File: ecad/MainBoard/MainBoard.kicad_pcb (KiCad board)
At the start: 2 copper layers, 34.6 x 88.7 mm, 44 parts, among them IC1 RC4558, J1 ACJM-HHDR, J2 ACJM-HHDR, J3 PJ-102A, Q1 2N4401BU, Q2 2N4401BU, SW1 FS57003PLT2B2M2QE

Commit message: Library recovery
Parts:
- C1: footprint Capacitor_SMD:C_0402_1005Metric_Pad0.74x0.62mm_HandSolder -> Capacitor_SMD:C_0805_2012Metric_Pad1.18x1.45mm_HandSolder; moved to F.Cu
- C10: value 0u1 -> 100n; footprint Capacitor_SMD:C_0201_0603Metric_Pad0.64x0.40mm_HandSolder -> Capacitor_SMD:C_0805_2012Metric_Pad1.18x1.45mm_HandSolder
- C11: footprint Capacitor_SMD:C_0603_1608Metric_Pad1.08x0.95mm_HandSolder -> Capacitor_SMD:C_0805_2012Metric_Pad1.18x1.45mm_HandSolder
- C12: footprint Capacitor_SMD:C_1210_3225Metric_Pad1.33x2.70mm_HandSolder -> screaming-panda:CAPPRD250W55D655H1220; moved to F.Cu
- C2, C8: footprint Capacitor_SMD:C_0603_1608Metric_Pad1.08x0.95mm_HandSolder -> Capacitor_SMD:C_0805_2012Metric_Pad1.18x1.45mm_HandSolder; moved to F.Cu
- C3: footprint Capacitor_SMD:C_0201_0603Metric_Pad0.64x0.40mm_HandSolder -> Capacitor_SMD:C_0805_2012Metric_Pad1.18x1.45mm_HandSolder
- C4: footprint Capacitor_SMD:C_0201_0603Metric_Pad0.64x0.40mm_HandSolder -> Capacitor_SMD:C_0805_2012Metric_Pad1.18x1.45mm_HandSolder; moved to F.Cu
- C5: value 0u22 -> 220n; footprint Capacitor_SMD:C_0402_1005Metric_Pad0.74x0.62mm_HandSolder -> Capacitor_SMD:C_0805_2012Metric_Pad1.18x1.45mm_HandSolder; moved to F.Cu
- C7: footprint Capacitor_SMD:C_1206_3216Metric_Pad1.33x1.80mm_HandSolder -> Capacitor_SMD:C_0805_2012Metric_Pad1.18x1.45mm_HandSolder; moved to F.Cu
- C9: footprint Capacitor_SMD:C_1206_3216Metric_Pad1.33x1.80mm_HandSolder -> Capacitor_SMD:C_0805_2012Metric_Pad1.18x1.45mm_HandSolder
- D1, D2: footprint Diode_THT:D_DO-35_SOD27_P2.54mm_Vertical_AnodeUp -> Diode_THT:D_DO-35_SOD27_P5.08mm_Vertical_KathodeUp
- D4: value QBL8XX60D -> LED_BLUE; footprint DigiKey:LED_5mm_Radial -> digikey-footprints:LED_5mm_Radial
- D5: footprint Diode_THT:D_DO-35_SOD27_P2.54mm_Vertical_AnodeUp -> Diode_THT:D_DO-35_SOD27_P7.62mm_Horizontal
- IC1: footprint DigiKey:SOIC-8_W3.9mm -> digikey-footprints:SOIC-8_W5.6mm; moved to F.Cu
- Q1: value 2N4401BU -> 2N4424; footprint DigiKey:TO-92-3 -> digikey-footprints:TO-92-3
- Q2: value 2N4401BU -> 2N4424; footprint DigiKey:TO-92-3 -> screaming-panda:TO-92-3_Formed_Leads
- R1, R17, R18, R22: footprint Resistor_SMD:R_0402_1005Metric_Pad0.72x0.64mm_HandSolder -> Resistor_SMD:R_0805_2012Metric_Pad1.20x1.40mm_HandSolder; moved to F.Cu
- R10, R13, R2, R3, R5, R9: moved to F.Cu
- R11: footprint Resistor_SMD:R_2512_6332Metric_Pad1.40x3.35mm_HandSolder -> Resistor_SMD:R_0805_2012Metric_Pad1.20x1.40mm_HandSolder
- R15: footprint Resistor_SMD:R_1218_3246Metric_Pad1.22x4.75mm_HandSolder -> Resistor_SMD:R_0805_2012Metric_Pad1.20x1.40mm_HandSolder
- R19, R20, R21: footprint Connector_PinHeader_2.54mm:PinHeader_1x03_P2.54mm_Vertical -> screaming-panda:75160-195-03LF
- R23, R8: footprint Resistor_SMD:R_0402_1005Metric_Pad0.72x0.64mm_HandSolder -> Resistor_SMD:R_0805_2012Metric_Pad1.20x1.40mm_HandSolder
- R7: footprint Resistor_SMD:R_1206_3216Metric_Pad1.30x1.75mm_HandSolder -> Resistor_SMD:R_0805_2012Metric_Pad1.20x1.40mm_HandSolder; moved to F.Cu
- moved IC1 175.1 mm to (118.9, -61.7), turned to 0 degrees
- moved SW1 164.0 mm to (93.9, -23.7)
- moved J1 161.0 mm to (72.1, -24.3)
- moved C11 148.2 mm to (56.1, 25.1), turned to 0 degrees
- moved R13 145.2 mm to (56.1, 28.1), turned to 0 degrees
- moved D2 145.1 mm to (25.1, 25.5), turned to 0 degrees
- moved C2 144.6 mm to (26.0, 32.6), turned to 0 degrees
- moved D1 142.5 mm to (25.1, 29.2)
- moved R5 137.1 mm to (40.2, 31.0), turned to 0 degrees
- moved C4 136.5 mm to (34.5, 25.1)
- moved R23 135.6 mm to (33.6, 44.2), turned to 0 degrees
- moved D4 134.0 mm to (28.6, 46.5)
- moved R16 132.2 mm to (30.7, 32.6)
- moved C3 132.1 mm to (34.5, 28.1), turned to 0 degrees
- moved R7 131.8 mm to (35.5, 31.1), turned to 0 degrees
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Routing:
- net +9V: track 77.7 -> 0.00 mm
- net /SIG_OUT: track 36.9 -> 0.00 mm
- net Net-(D4-Pad1): track 33.9 -> 0.00 mm
- net /PassThru: track 20.1 -> 0.00 mm
- net 0: track 18.3 -> 0.00 mm
- net Net-(SW1-Pad3): track 5.30 -> 0.00 mm
- net Net-(D4-Pad2): track 4.98 -> 0.00 mm
- removed copper zone on F.Cu, net 0
- removed copper zone on B.Cu, net VCC
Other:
- outline, holes or cut-outs redrawn

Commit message: PCB layout after data loss
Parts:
- C1, C11, C2, C4, C5, C8, IC1, R1, R13, R14, R15, R17, R18, R2, R22, R23, R3, R5, R8: moved to B.Cu
- Q2: footprint screaming-panda:TO-92-3_Formed_Leads -> digikey-footprints:TO-92-3
- moved SW1 158.9 mm to (100.1, 135.0), turned to 180 degrees
- moved IC1 157.6 mm to (100.4, 94.8), turned to 180 degrees
- moved Q2 155.9 mm to (85.4, 124.7), turned to 90 degrees
- moved J1 145.6 mm to (100.7, 118.4)
- moved R21 118.4 mm to (97.5, 83.9)
- moved D1 114.9 mm to (114.6, 101.4), turned to 270 degrees
- moved D2 112.5 mm to (114.6, 93.7), turned to 270 degrees
- moved J2 110.6 mm to (99.3, 100.2), turned to 180 degrees
- moved C11 109.6 mm to (91.0, 129.0)
- moved R13 107.2 mm to (96.4, 127.4), turned to 90 degrees
- moved R14 106.6 mm to (93.2, 126.6)
- moved R12 103.4 mm to (85.2, 128.8), turned to 90 degrees
- moved R20 102.0 mm to (97.5, 79.9)
- moved C4 102.0 mm to (102.8, 100.8)
- moved C12 101.8 mm to (100.0, 72.4), turned to 270 degrees
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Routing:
- net +9V: track 0.00 -> 108.7 mm, vias 0 -> 1
- net /SIG_OUT: track 0.00 -> 62.6 mm
- net Net-(C3-Pad1): track 0.00 -> 54.9 mm
- net Net-(C4-Pad2): track 0.00 -> 44.4 mm, vias 0 -> 1
- net /PassThru: track 0.00 -> 43.2 mm
- net Net-(C10-Pad2): track 0.00 -> 40.6 mm
- net Net-(IC1-Pad6): track 0.00 -> 28.7 mm
- net /tone/IN: track 0.00 -> 25.5 mm
- net Net-(Q1-Pad2): track 0.00 -> 23.4 mm, vias 0 -> 1
- net /drive/IN: track 0.00 -> 22.1 mm
- net Net-(D4-Pad1): track 0.00 -> 21.5 mm
- net 0: track 0.00 -> 15.8 mm
- net /volume/IN: track 0.00 -> 13.4 mm
- net Net-(C10-Pad1): track 0.00 -> 11.1 mm
- net Net-(D4-Pad2): track 0.00 -> 8.50 mm
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- added copper zone on B.Cu, net 0
- added copper zone on F.Cu, net VCC

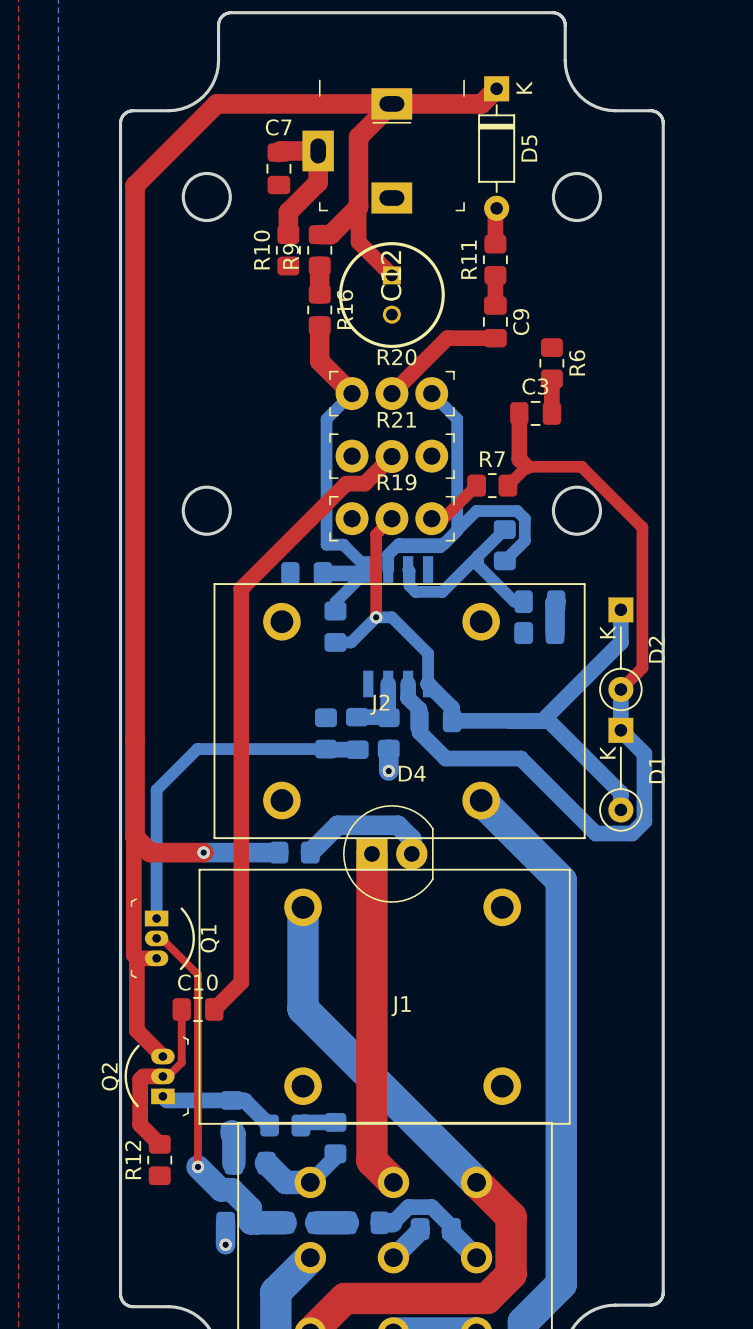
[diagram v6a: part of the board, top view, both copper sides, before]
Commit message: Layout all components, first revision
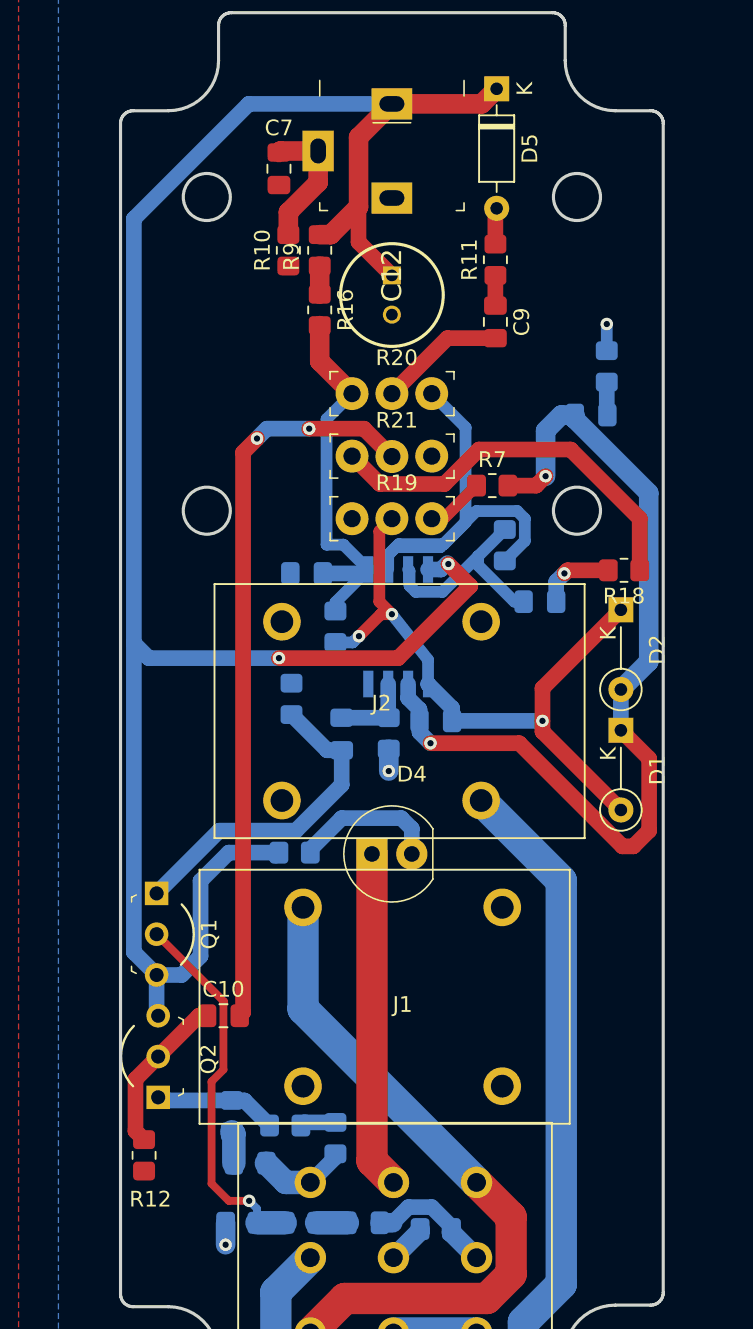
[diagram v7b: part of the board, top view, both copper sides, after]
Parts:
- C3, R6: moved to B.Cu
- Q1, Q2: footprint digikey-footprints:TO-92-3 -> digikey-footprints:TO-92-3_Formed_Leads
- R18: moved to F.Cu
- moved R18 6.72 mm to (114.8, 91.2), turned to 180 degrees
- moved C3 3.54 mm to (112.7, 81.3)
- moved R6 3.51 mm to (113.7, 78.2)
- moved R3 3.11 mm to (93.6, 99.4)
- moved C10 1.67 mm to (89.3, 119.6)
- moved Q1 1.60 mm to (85.0, 111.8)
- moved R12 1.04 mm to (84.2, 128.5)
- moved C2 1.00 mm to (96.8, 101.6)
- moved Q2 0.31 mm to (85.1, 124.8)
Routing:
- net +9V: track 108.7 -> 135.2 mm, vias 1 -> 2
- net Net-(R18-Pad1): track 0.00 -> 25.1 mm
- net Net-(C10-Pad2): track 40.6 -> 46.9 mm, vias 0 -> 2
- net Net-(C3-Pad1): track 54.9 -> 59.2 mm, vias 0 -> 2
- net Net-(C8-Pad2): track 2.03 -> 4.90 mm, vias 0 -> 1
- net Net-(C4-Pad2): track 44.4 -> 42.3 mm, vias 1 -> 3
- net VCC: track 4.60 -> 6.30 mm, vias 2 -> 3
- net /drive/IN: track 22.1 -> 21.0 mm
- net Net-(C2-Pad2): track 4.18 -> 5.16 mm
- net Net-(D4-Pad2): track 8.50 -> 9.39 mm
- net Net-(Q1-Pad2): track 23.4 -> 24.3 mm
- net Net-(C10-Pad1): track 11.1 -> 10.3 mm

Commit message: Fix DRC issues
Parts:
- R7: moved to B.Cu
- moved R7 0.45 mm to (106.6, 85.4)
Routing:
- net Net-(IC1-Pad6): track 29.1 -> 24.7 mm
- net Net-(C3-Pad1): track 59.2 -> 58.2 mm, vias 2 -> 1
- net Net-(C4-Pad2): track 42.3 -> 43.0 mm
- net Net-(R18-Pad1): track 25.1 -> 25.2 mm, vias 0 -> 1
